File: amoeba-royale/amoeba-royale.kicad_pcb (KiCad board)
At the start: 2 copper layers, 18.8 x 18.1 mm, 48 parts

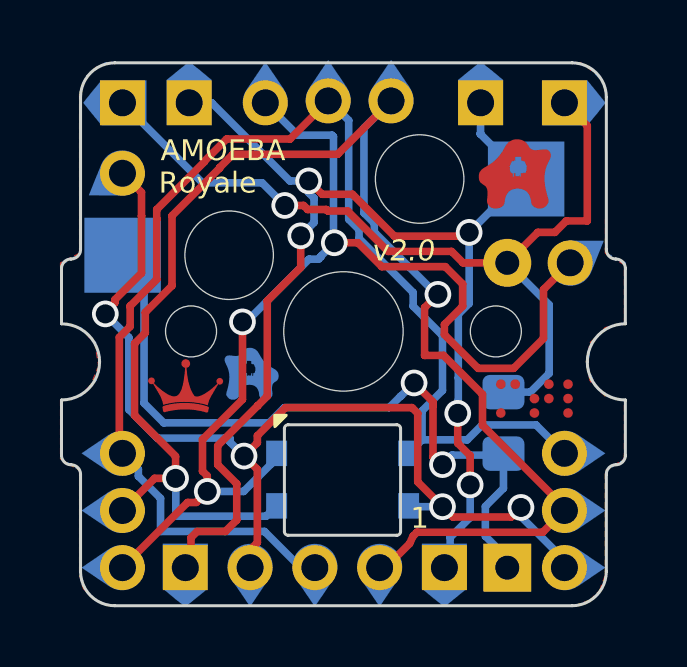
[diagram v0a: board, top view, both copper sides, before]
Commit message: Remove tear pads for jlcpcb
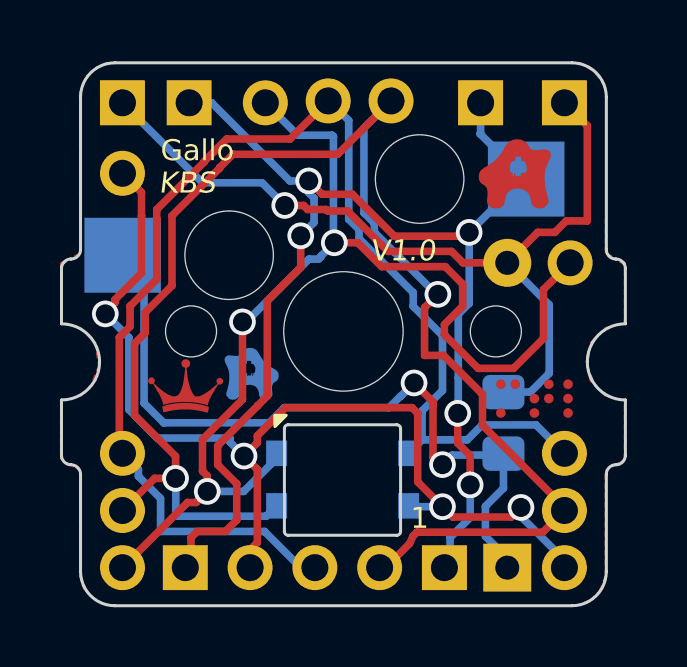
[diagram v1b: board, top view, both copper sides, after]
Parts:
- removed pad-arrow-round (x12): G***, pad-arrow-round
- removed pad-arrow-round.34b (x2): G***, amoeba-modules:pad-arrow-round.34b
- removed pad-arrow-square (x6): G***, pad-arrow-square
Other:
- board text added: "Gallo"
- board text added: "KBS"
- board text added: "V1.0"
- board text removed: "AMOEBA"
- board text removed: "Royale"
- board text removed: "v2.0"
